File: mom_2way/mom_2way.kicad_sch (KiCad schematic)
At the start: 8 parts, among them J1 I/O connector

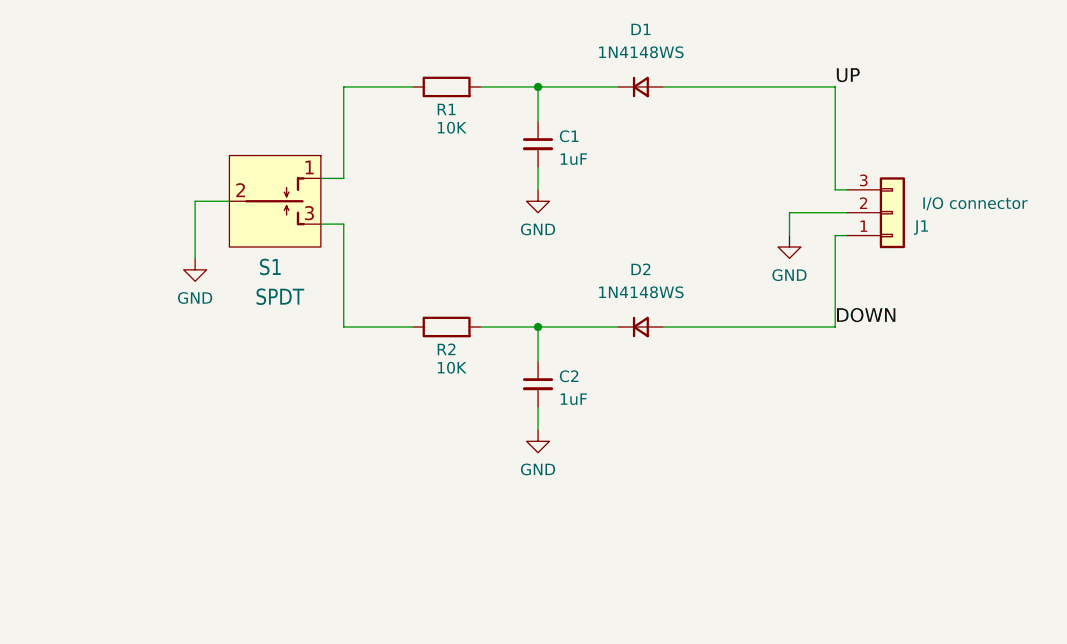
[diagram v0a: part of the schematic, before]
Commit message: 2-Way Switch refinements
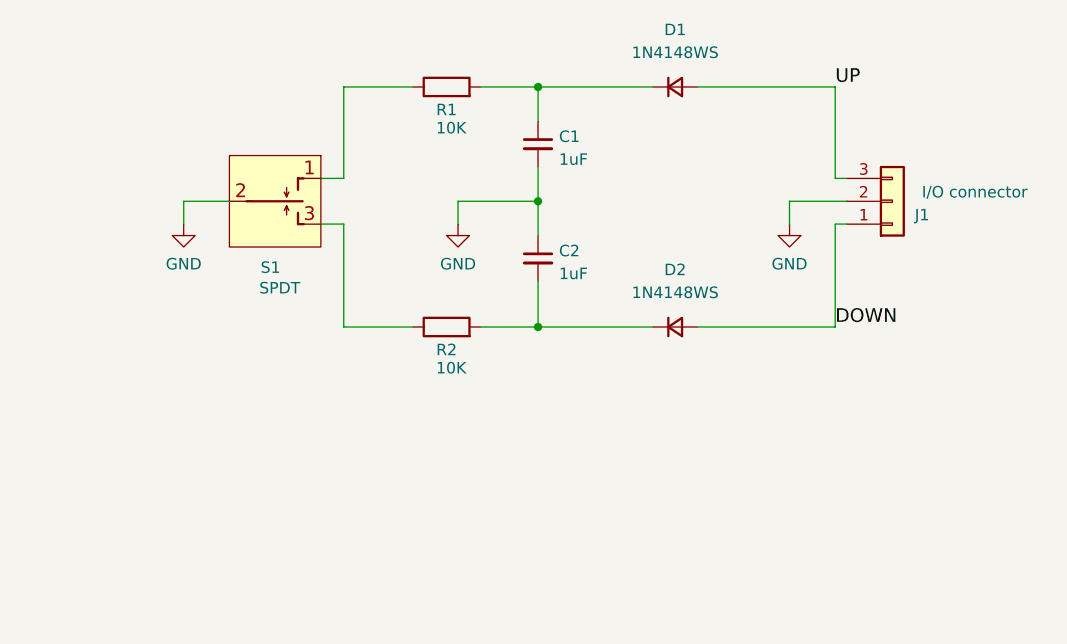
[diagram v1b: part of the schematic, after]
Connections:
- net GND: now also C2.1; no longer C2.2
- net at D2.1 (K), R2.2: now also C2.2; no longer C2.1
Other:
- moved on the sheet: C2, D1, D2, J1

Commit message: Cleanup and refinements
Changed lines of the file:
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@@
+	)
+	(symbol
+		(lib_id "power:PWR_FLAG")
+		(at 140.97 86.36 270)
+		(unit 1)
+		(exclude_from_sim no)
+		(in_bom yes)
+		(on_board yes)
+		(dnp no)
+		(fields_autoplaced yes)
+		(property "Reference" "#FLG01"
+			(at 142.875 86.36 0)
+			(effects
+				(font
+					(size 1.27 1.27)
+				)
+				(hide yes)
+			)
+		)
+		(property "Value" "PWR_FLAG"
+			(at 144.78 86.3599 90)
+			(effects
+				(font
+					(size 1.27 1.27)
+				)
+				(justify left)
+				(hide yes)
+			)
+		)
+		(property "Footprint" ""
+			(at 140.97 86.36 0)
+			(effects
+				(font
+					(size 1.27 1.27)
+				)
+				(hide yes)
+			)
+		)
+		(property "Datasheet" "~"
+			(at 140.97 86.36 0)
+			(effects
+				(font
+					(size 1.27 1.27)
+				)
+				(hide yes)
+			)
+		)
+		(property "Description" "Special symbol for telling ERC where power comes from"
+			(at 140.97 86.36 0)
+			(effects
+				(font
+					(size 1.27 1.27)
+				)
+				(hide yes)
+			)
+		)
+		(pin "1"
+		)
+		(instances
+			(project ""
+				(path "/e63e39d7-6ac0-4ffd-8aa3-1841a4541b55"
+					(reference "#FLG01")
+					(unit 1)
+				)
+			)
+		)
 	)
 	(symbol
